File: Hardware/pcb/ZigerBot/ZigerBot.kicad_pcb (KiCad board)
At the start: 2 copper layers, 34 parts, among them J1 Screw_Terminal_01x03, J2 Screw_Terminal_01x02, J3 Screw_Terminal_01x02, U1 L7805, U2 NXP 74HC04, U3 L298P

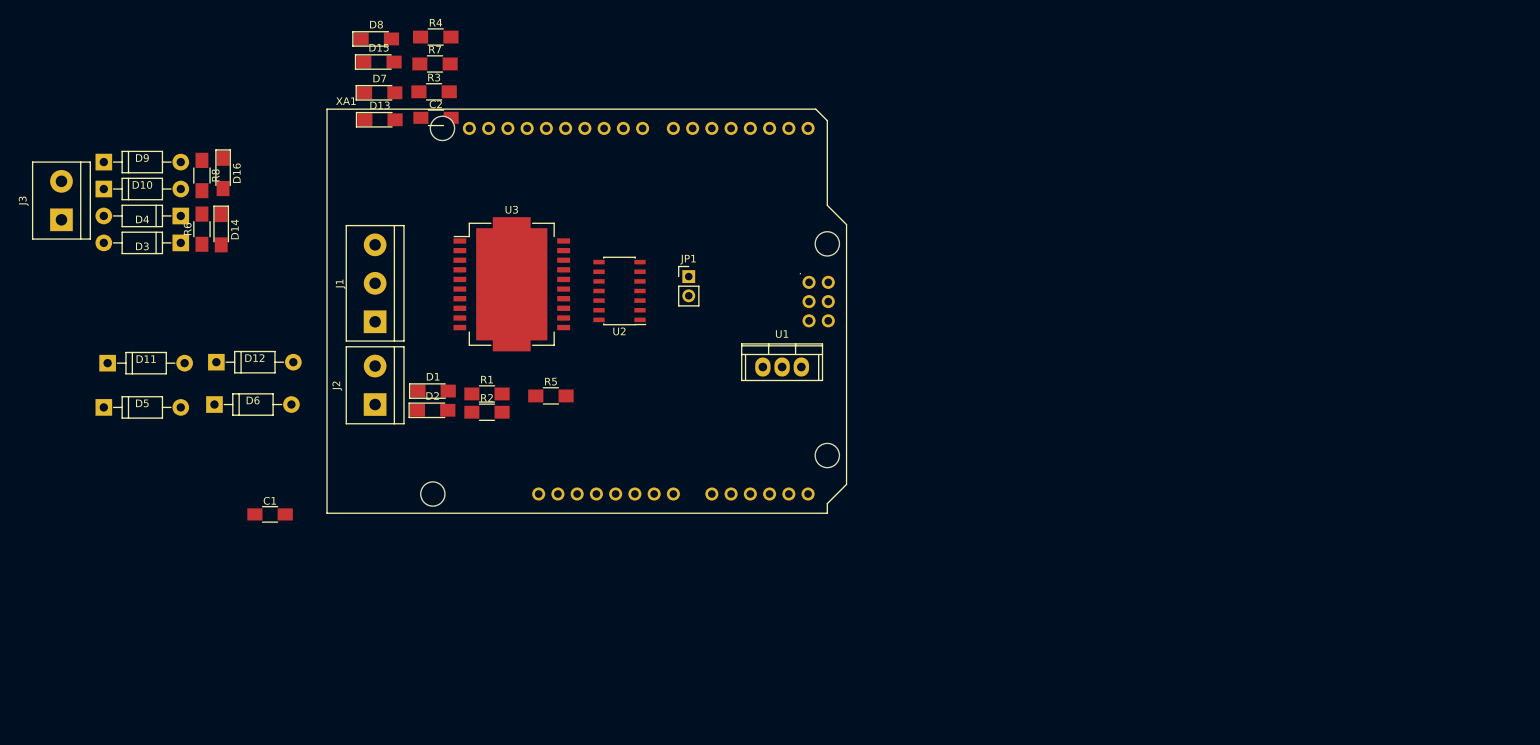
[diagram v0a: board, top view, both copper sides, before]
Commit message: PCB erweitert
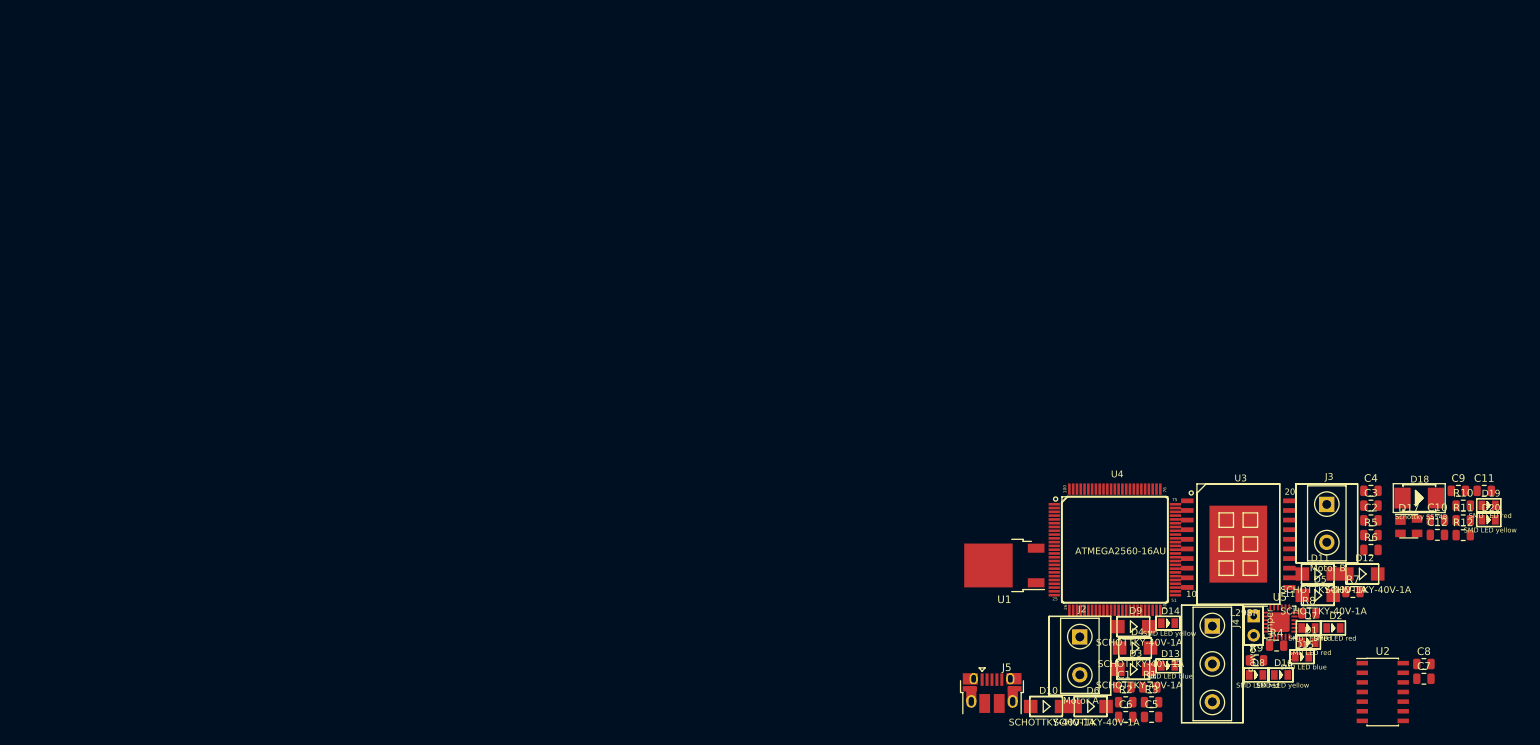
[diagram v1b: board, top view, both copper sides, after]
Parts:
- removed JP1: Jumper, Pin_Headers:Pin_Header_Straight_1x02_Pitch2.54mm
- removed XA1: Arduino_Uno_Shield, Arduino:Arduino_Uno_Shield
- added C10: 0.1uF, Capacitor_SMD:C_0805_2012Metric, F.Cu at (188.7, 87.4)
- added C11: 0.1uF, Capacitor_SMD:C_0805_2012Metric, F.Cu at (194.9, 83.5)
- added C12: 0.1uF, Capacitor_SMD:C_0805_2012Metric, F.Cu at (188.7, 89.3)
- added C3: 4.7uF, Capacitor_SMD:C_0805_2012Metric, F.Cu at (180.0, 85.5)
- added C4: 0.1uF, Capacitor_SMD:C_0805_2012Metric, F.Cu at (180.0, 83.5)
- added C5: 0.1uF, Capacitor_SMD:C_0805_2012Metric, F.Cu at (151.0, 113.4)
- added C6: 4.7uF, Capacitor_SMD:C_0805_2012Metric, F.Cu at (147.6, 113.4)
- added C7: 0.33uF, Capacitor_SMD:C_0805_2012Metric, F.Cu at (187.0, 108.3)
- added C8: 0.1uF, Capacitor_SMD:C_0805_2012Metric, F.Cu at (187.0, 106.4)
- added C9: 0.1uF, Capacitor_SMD:C_0805_2012Metric, F.Cu at (191.5, 83.5)
- added D17: SP0503BAHT, Package_TO_SOT_SMD:SOT-143, F.Cu at (185.0, 88.2)
- added D18: Schottky SS54B, SeeedOPL-Diode:DO-214AA, F.Cu at (186.3, 84.5)
- added D19: SMD LED red, SeeedOPL-LED:LED-0805, F.Cu at (195.5, 85.5)
- added D20: SMD LED yellow, SeeedOPL-LED:LED-0805, F.Cu at (195.5, 87.4)
- added J4: Jumper, SeeedOPL-Connector:H2-2.54, F.Cu at (164.5, 101.3)
- added J5: USB_B_Micro, Connector_USB:USB_Micro-B_Amphenol_10103594-0001LF_Horizontal, F.Cu at (130.0, 110.2)
- added R10: 10k, Resistor_SMD:R_0805_2012Metric, F.Cu at (192.1, 85.5)
- added R11: 10k, Resistor_SMD:R_0805_2012Metric, F.Cu at (192.1, 87.4)
- added R12: 10k, Resistor_SMD:R_0805_2012Metric, F.Cu at (192.1, 89.4)
- added R9: 1k, Resistor_SMD:R_0805_2012Metric, F.Cu at (164.9, 105.9)
- added U4: ATMEGA2560-16AU, SeeedOPL-IC:TQFP100-0.5-14X14MM, F.Cu at (146.2, 91.3)
- added U5: CP2102N-A01-GQFN24, Package_DFN_QFN:QFN-24-1EP_4x4mm_P0.5mm_EP2.6x2.6mm, F.Cu at (167.9, 100.9)
- C1, C2: value 0.1uF C1206S104M5RACTU -> 0.1uF; footprint Capacitors_SMD:C_1206_HandSoldering -> Capacitor_SMD:C_0805_2012Metric
- D1: value LED Blue -> SMD LED red; footprint LEDs:LED_1206_HandSoldering -> SeeedOPL-LED:LED-0805
- D10, D11, D12, D3, D4, D5, D6, D9: value SR140 -> SCHOTTKY-40V-1A; footprint ZigerBot:D_DO-41_SOD81_P10.16mm_Horizontal -> SeeedOPL-Diode:DO-214AC
- D13, D15: value LED Red -> SMD LED blue; footprint LEDs:LED_1206_HandSoldering -> SeeedOPL-LED:LED-0805
- D14: value LED BLUE -> SMD LED yellow; footprint LEDs:LED_1206_HandSoldering -> SeeedOPL-LED:LED-0805
- D16: value LED Yellow -> SMD LED yellow; footprint LEDs:LED_1206_HandSoldering -> SeeedOPL-LED:LED-0805
- D2: value LED Yellow -> SMD LED red; footprint LEDs:LED_1206_HandSoldering -> SeeedOPL-LED:LED-0805
- D7, D8: value LED Red -> SMD LED red; footprint LEDs:LED_1206_HandSoldering -> SeeedOPL-LED:LED-0805
- J1: value Screw_Terminal_01x03 -> Power; footprint Connectors_Terminal_Blocks:TerminalBlock_bornier-3_P5.08mm -> SeeedOPL-Connector:H3-5.0-15.5X8.0MM
- J2: value Screw_Terminal_01x02 -> Motor A; footprint Connectors_Terminal_Blocks:TerminalBlock_bornier-2_P5.08mm -> SeeedOPL-Connector:H2-5.0-10.5X8.0MM
- J3: value Screw_Terminal_01x02 -> Motor B; footprint Connectors_Terminal_Blocks:TerminalBlock_bornier-2_P5.08mm -> SeeedOPL-Connector:H2-5.0-10.5X8.0MM
- R1, R2, R3, R4, R5, R6, R7, R8: footprint Resistors_SMD:R_1206_HandSoldering -> Resistor_SMD:R_0805_2012Metric
- U1: value L7805 -> L7805CV; footprint Power_Integrations:TO-220 -> Package_TO_SOT_SMD:TO-252-2
- U2: footprint Housings_SOIC:SOIC-14_3.9x8.7mm_Pitch1.27mm -> Package_SO:SOIC-14_3.9x8.7mm_P1.27mm
- U3: footprint Housings_SOIC:HSOP-20-1EP_11.0x15.9mm_Pitch1.27mm_SlugDown -> SeeedOPL-IC:SOIC20G-1.27-16X11MM
- moved J3 171.8 mm to (174.1, 87.8), turned to 0 degrees
- moved D5 162.2 mm to (172.9, 97.3)
- moved D11 162.1 mm to (172.9, 94.5)
- moved R6 160.0 mm to (180.0, 91.3), turned to 0 degrees
- moved R8 157.1 mm to (171.8, 99.7), turned to 0 degrees
- moved D16 154.6 mm to (168.1, 107.8), turned to 0 degrees
- moved D12 153.8 mm to (178.8, 94.5)
- moved D9 149.1 mm to (148.6, 101.5)
- moved D15 145.0 mm to (170.9, 105.4)
- moved D8 143.3 mm to (164.8, 107.8)
- moved D10 141.9 mm to (137.1, 112.0)
- moved D7 141.5 mm to (171.7, 101.6)
- moved R7 139.8 mm to (177.6, 96.9)
- moved D4 138.3 mm to (148.8, 104.3), turned to 0 degrees
- moved D3 137.8 mm to (148.6, 107.1), turned to 0 degrees
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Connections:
- C1 pad 1: VSS -> GND
- C1 pad 2: GND -> /VSS
- C2 pad 1: /VS -> Net-(C2-Pad1)
- C2 pad 2: GND -> /VSS
- D10 pad 2: GND -> Net-(D10-Pad2)
- D11 pad 1: Net-(D1-Pad1) -> GND
- D11 pad 2: GND -> Net-(D11-Pad2)
- D12 pad 1: Net-(D12-Pad1) -> Net-(D11-Pad2)
- D12 pad 2: GND -> /VSS
- D3 pad 1: VSS -> GND
- D3 pad 2: Net-(D14-Pad1) -> Net-(D15-Pad-)
- D4 pad 1: VSS -> Net-(D15-Pad-)
- D4 pad 2: Net-(D10-Pad1) -> /VSS
- D5 pad 1: VSS -> GND
- D5 pad 2: Net-(D1-Pad1) -> Net-(D5-Pad2)
- D6 pad 1: VSS -> Net-(D5-Pad2)
- D6 pad 2: Net-(D12-Pad1) -> Net-(D6-Pad2)
- D9 pad 1: Net-(D14-Pad1) -> GND
- D9 pad 2: GND -> Net-(D10-Pad1)
- J1 pad 2: VSS -> /VSS
- J2 pad 1: Net-(D12-Pad1) -> Net-(D11-Pad2)
- J2 pad 2: Net-(D1-Pad1) -> Net-(D10-Pad1)
- J3 pad 1: Net-(D10-Pad1) -> Net-(D5-Pad2)
- J3 pad 2: Net-(D14-Pad1) -> Net-(D15-Pad-)
- R1 pad 1: Net-(D1-Pad2) -> /DirMotA
- R1 pad 2: Net-(D12-Pad1) -> Net-(D1-Pad+)
- R2 pad 1: Net-(D12-Pad1) -> /EnaMotA
- R2 pad 2: Net-(D2-Pad1) -> Net-(D2-Pad+)
- R3 pad 1: Net-(D7-Pad2) -> /DirMotB
- R3 pad 2: /D2 -> Net-(D7-Pad+)
- R4 pad 1: Net-(D8-Pad2) -> /EnaMotB
- R4 pad 2: /D3 -> Net-(D8-Pad+)
- R5 pad 1: Net-(D13-Pad2) -> Net-(D11-Pad2)
- R5 pad 2: /D4 -> Net-(D13-Pad+)
- R6 pad 1: Net-(D14-Pad2) -> Net-(D11-Pad2)
- R6 pad 2: Net-(D10-Pad1) -> Net-(D14-Pad-)
- R7 pad 1: Net-(D15-Pad2) -> Net-(D5-Pad2)
- R7 pad 2: /D11 -> Net-(D15-Pad+)
- R8 pad 1: Net-(D16-Pad1) -> Net-(D5-Pad2)
- R8 pad 2: Net-(D10-Pad1) -> Net-(D16-Pad-)
- U1 pad 3: VSS -> /VSS
- U2 pad 1: /D2 -> /DirMotA
- U2 pad 14: VSS -> /VSS
- U2 pad 3: /D4 -> /DirMotB
- U3 pad 12: VSS -> /VSS
- U3 pad 13: /D4 -> /DirMotB
- U3 pad 14: /D11 -> /EnaMotB
- U3 pad 16: Net-(D10-Pad1) -> Net-(D5-Pad2)
- U3 pad 17: Net-(D14-Pad1) -> Net-(D15-Pad-)
- U3 pad 4: Net-(D12-Pad1) -> Net-(D11-Pad2)
- U3 pad 5: Net-(D1-Pad1) -> Net-(D10-Pad1)
- U3 pad 6: /VS -> Net-(C4-Pad2)
- U3 pad 7: /D2 -> /DirMotA
- U3 pad 8: /D3 -> /EnaMotA
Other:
- rule pad_to_mask_clearance: 0.2 -> 0

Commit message: PCB changed
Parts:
- removed J5: USB_B_Micro, Connector_USB:USB_Micro-B_Amphenol_10103594-0001LF_Horizontal
- removed U1: L7805CV, Package_TO_SOT_SMD:TO-252-2
- removed U2: NXP 74HC04, Package_SO:SOIC-14_3.9x8.7mm_P1.27mm
- removed U5: CP2102N-A01-GQFN24, Package_DFN_QFN:QFN-24-1EP_4x4mm_P0.5mm_EP2.6x2.6mm
- added BZ1: Buzzer CEM-1203(42), ZigerBot:BUZZER_CEM-1203(24)_12mm_6.5mm_0.6mm, F.Cu at (43.7, 126.0)
- added C13: 100nF, Capacitors_SMD:C_0402, F.Cu at (146.5, 79.7)
- added C14: 100nF, Capacitors_SMD:C_0402, F.Cu at (149.5, 79.7)
- added C15: 100nF, Capacitors_SMD:C_0402, F.Cu at (160.1, 69.2)
- added C16: 100nF, Capacitors_SMD:C_0402, F.Cu at (152.4, 80.7)
- added C17: 100nF, Capacitors_SMD:C_0402, F.Cu at (163.1, 69.2)
- added C18: 100nF, Capacitors_SMD:C_0402, F.Cu at (160.1, 72.7)
- added C19: 100nF, Capacitors_SMD:C_0402, F.Cu at (148.4, 83.1)
- added C20: 100nF, Capacitors_SMD:C_0402, F.Cu at (140.7, 88.8)
- added C21: 0.1uF, Capacitors_SMD:C_0402, F.Cu at (143.7, 86.5)
- added C22: 4.7uF, Capacitors_SMD:C_0402, F.Cu at (137.8, 92.2)
- added C23: 100nF, Capacitors_SMD:C_0402, F.Cu at (156.3, 68.2)
- added C24: 100nF, Capacitors_SMD:C_0402, F.Cu at (134.8, 91.2)
- added C25: 100nF, Capacitors_SMD:C_0402, F.Cu at (149.6, 76.2)
- added C26: 100nF, Capacitors_SMD:C_0402, F.Cu at (145.4, 83.1)
- added C27: 100nF, Capacitors_SMD:C_0402, F.Cu at (140.5, 78.6)
- added C28: 100nF, Capacitors_SMD:C_0402, F.Cu at (131.8, 91.2)
- added C29: 100nF, Capacitors_SMD:C_0402, F.Cu at (149.6, 72.8)
- added C30: 100nF, Capacitors_SMD:C_0402, F.Cu at (143.5, 79.7)
- added C31: 100nF, Capacitors_SMD:C_0402, F.Cu at (146.6, 76.2)
- added C32: 100nF, Capacitors_SMD:C_0402, F.Cu at (161.0, 62.4)
- added C33: 0.1uF, Capacitors_SMD:C_0402, F.Cu at (164.1, 59.0)
- added C34: 4.7uF, Capacitors_SMD:C_0402, F.Cu at (140.5, 82.0)
- added C35: 100nF, Capacitors_SMD:C_0402, F.Cu at (158.0, 64.7)
- added C36: 100nF, Capacitors_SMD:C_0402, F.Cu at (135.8, 87.7)
- added C37: 100nF, Capacitors_SMD:C_0402, F.Cu at (153.3, 70.5)
- added C38: 100nF, Capacitors_SMD:C_0402, F.Cu at (125.9, 90.7)
- added C39: 100nF, Capacitors_SMD:C_0402, F.Cu at (158.0, 61.3)
- added D21: WS2812B, ZigerBot:LED_WS2812B-PLCC4, F.Cu at (200.2, 81.5)
- added D22: WS2812B, ZigerBot:LED_WS2812B-PLCC4, F.Cu at (208.0, 81.5)
- added D24: WS2812B, ZigerBot:LED_WS2812B-PLCC4, F.Cu at (176.5, 89.2)
- added D25: WS2812B, ZigerBot:LED_WS2812B-PLCC4, F.Cu at (184.4, 89.2)
- added D26: WS2812B, ZigerBot:LED_WS2812B-PLCC4, F.Cu at (192.3, 89.2)
- added D27: WS2812B, ZigerBot:LED_WS2812B-PLCC4, F.Cu at (200.2, 89.2)
- added D28: WS2812B, ZigerBot:LED_WS2812B-PLCC4, F.Cu at (208.0, 89.2)
- added D29: WS2812B, ZigerBot:LED_WS2812B-PLCC4, F.Cu at (176.5, 96.8)
- added D30: WS2812B, ZigerBot:LED_WS2812B-PLCC4, F.Cu at (184.4, 96.8)
- added D31: WS2812B, ZigerBot:LED_WS2812B-PLCC4, F.Cu at (192.3, 96.8)
- added D32: WS2812B, ZigerBot:LED_WS2812B-PLCC4, F.Cu at (200.2, 96.8)
- added D33: WS2812B, ZigerBot:LED_WS2812B-PLCC4, F.Cu at (208.0, 96.8)
- added J6: 3 Pin Male Servo Header, Pin_Headers:Pin_Header_Straight_1x03_Pitch2.54mm, F.Cu at (177.3, 112.3)
- added J7: 3 Pin Male Servo Header, Pin_Headers:Pin_Header_Straight_1x03_Pitch2.54mm, F.Cu at (189.0, 112.3)
- added J8: 3 Pin Male Servo Header, Pin_Headers:Pin_Header_Straight_1x03_Pitch2.54mm, F.Cu at (199.9, 112.3)
- added J9: 3 Pin Male Servo Header, Pin_Headers:Pin_Header_Straight_1x03_Pitch2.54mm, F.Cu at (209.6, 112.3)
- added JP1: Jumper, Pin_Headers:Pin_Header_Straight_1x03_Pitch2.54mm, F.Cu at (112.3, 68.3)
- added Q1: SMD-MOSFET-P-CH-20V-2A-FDN340P_SOT-23_, TO_SOT_Packages_SMD:SOT-23, F.Cu at (82.4, 87.0)
- added RV1: Potentiometer, Potentiometers:Potentiometer_Trimmer-EVM3E, F.Cu at (136.8, 79.5)
- added RV2: Potentiometer, Potentiometers:Potentiometer_Trimmer-EVM3E, F.Cu at (154.3, 62.2)
- added SW1: SMD Button, Buttons_Switches_SMD:SW_SPST_SKQG, F.Cu at (113.8, 106.7)
- added SW2: SMD Button, Buttons_Switches_SMD:SW_SPST_SKQG, F.Cu at (104.9, 106.7)
- added SW3: SMD Button, Buttons_Switches_SMD:SW_SPST_SKQG, F.Cu at (122.7, 106.7)
- added SW4: SMD Button, Buttons_Switches_SMD:SW_SPST_SKQG, F.Cu at (131.3, 106.7)
- added Y1: 16MHz Resonator, ZigerBot:Resonator_SMD_muRata_CSTNE16M0V530000_3pin_3.2x1.3x0.9mm, F.Cu at (82.5, 84.1)
- C1, C10, C8, C9: footprint Capacitor_SMD:C_0805_2012Metric -> Capacitors_SMD:C_0402
- C11, C12: value 0.1uF -> 100nF; footprint Capacitor_SMD:C_0805_2012Metric -> Capacitors_SMD:C_0402
- C2: value 0.1uF -> 0.33uF; footprint Capacitor_SMD:C_0805_2012Metric -> Capacitors_SMD:C_0402
- C3: value 4.7uF -> 0.1uF; footprint Capacitor_SMD:C_0805_2012Metric -> Capacitors_SMD:C_0402
- C4: value 0.1uF -> 0.1 uF; footprint Capacitor_SMD:C_0805_2012Metric -> Capacitors_SMD:C_0402
- C5: value 0.1uF -> 10uF 16V; footprint Capacitor_SMD:C_0805_2012Metric -> Capacitors_SMD:C_0402
- C6: value 4.7uF -> 10uF 16V; footprint Capacitor_SMD:C_0805_2012Metric -> Capacitors_SMD:C_0402
- C7: value 0.33uF -> 10uF 16V; footprint Capacitor_SMD:C_0805_2012Metric -> Capacitors_SMD:C_0402
- D1: footprint SeeedOPL-LED:LED-0805 -> ZigerBot:LED_0603
- D10, D11, D12, D9: value SCHOTTKY-40V-1A -> WS2812B; footprint SeeedOPL-Diode:DO-214AC -> ZigerBot:LED_WS2812B-PLCC4
- D13, D15: value SMD LED blue -> WS2812B; footprint SeeedOPL-LED:LED-0805 -> ZigerBot:LED_WS2812B-PLCC4
- D14, D16, D20: value SMD LED yellow -> WS2812B; footprint SeeedOPL-LED:LED-0805 -> ZigerBot:LED_WS2812B-PLCC4
- D17: value SP0503BAHT -> WS2812B; footprint Package_TO_SOT_SMD:SOT-143 -> ZigerBot:LED_WS2812B-PLCC4
- D18: value Schottky SS54B -> WS2812B; footprint SeeedOPL-Diode:DO-214AA -> ZigerBot:LED_WS2812B-PLCC4
- D19, D8: value SMD LED red -> WS2812B; footprint SeeedOPL-LED:LED-0805 -> ZigerBot:LED_WS2812B-PLCC4
- D2: value SMD LED red -> SMD LED blue; footprint SeeedOPL-LED:LED-0805 -> ZigerBot:LED_0603
- D3, D4: value SCHOTTKY-40V-1A -> SMD LED yellow; footprint SeeedOPL-Diode:DO-214AC -> ZigerBot:LED_0603
- D5: value SCHOTTKY-40V-1A -> SMD LED green FAULT; footprint SeeedOPL-Diode:DO-214AC -> ZigerBot:LED_0603
- D6: value SCHOTTKY-40V-1A -> SMD LED blue; footprint SeeedOPL-Diode:DO-214AC -> ZigerBot:LED_0603
- D7: value SMD LED red -> SMD LED yellow; footprint SeeedOPL-LED:LED-0805 -> ZigerBot:LED_0603
- J1: value Power -> Motor A; footprint SeeedOPL-Connector:H3-5.0-15.5X8.0MM -> SeeedOPL-Connector:H2-5.0-10.5X8.0MM
- J2: value Motor A -> M Power
- J4: value Jumper -> 4 Pin Male SR-04 Header; footprint SeeedOPL-Connector:H2-2.54 -> SeeedOPL-Connector:H4-2.54
- R1: value 1k -> 100 Ohm; footprint Resistor_SMD:R_0805_2012Metric -> Resistors_SMD:R_0402
- R10, R11, R12: value 10k -> 1k; footprint Resistor_SMD:R_0805_2012Metric -> Resistors_SMD:R_0402
- R2, R3, R6, R9: value 1k -> 10k; footprint Resistor_SMD:R_0805_2012Metric -> Resistors_SMD:R_0402
- R4, R5: footprint Resistor_SMD:R_0805_2012Metric -> Resistors_SMD:R_0402
- R7, R8: value 1k -> 0.2 Ohm; footprint Resistor_SMD:R_0805_2012Metric -> Resistors_SMD:R_0402
- U3: value L298P -> ATmega2560-16AU; footprint SeeedOPL-IC:SOIC20G-1.27-16X11MM -> SeeedOPL-IC:TQFP100-0.5-14X14MM
- U4: value ATMEGA2560-16AU -> CP2102N-A01-GQFN24; footprint SeeedOPL-IC:TQFP100-0.5-14X14MM -> Housings_DFN_QFN:QFN-24-1EP_4x4mm_Pitch0.5mm
- moved R5 77.8 mm to (102.7, 80.8)
- moved D1 77.3 mm to (95.1, 93.4)
- moved D7 73.8 mm to (98.4, 93.4)
- moved D10 71.7 mm to (192.3, 66.3)
- moved J3 70.3 mm to (231.6, 47.5)
- moved J1 61.0 mm to (150.6, 45.9)
- moved J4 61.0 mm to (120.5, 59.0)
- moved C8 60.2 mm to (128.8, 90.7)
- moved C7 53.9 mm to (143.6, 76.2)
- moved R2 51.5 mm to (163.4, 62.4)
- moved U3 50.4 mm to (191.0, 49.0)
- moved D9 50.2 mm to (184.4, 66.3)
- moved J2 47.5 mm to (97.6, 87.1)
- moved C3 47.1 mm to (132.9, 84.3)
- moved D16 46.7 mm to (200.2, 73.9)
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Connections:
- C1 pad 1: GND -> Net-(C1-Pad1)
- C1 pad 2: /VSS -> /DTRmega
- C10 pad 2: Net-(C10-Pad2) -> 5V
- C11 pad 1: Net-(C11-Pad1) -> GND
- C11 pad 2: Net-(C10-Pad2) -> 5V
- C12 pad 2: Net-(C10-Pad2) -> 5V
- C2 pad 2: /VSS -> Net-(C2-Pad2)
- C3 pad 1: Net-(C2-Pad1) -> 5V
- C3 pad 2: /VSS -> Net-(C2-Pad1)
- C4 pad 1: GND -> /VCP
- C5 pad 1: Net-(C2-Pad1) -> Net-(C4-Pad2)
- C5 pad 2: Net-(C5-Pad2) -> Net-(C2-Pad1)
- C6 pad 1: Net-(C2-Pad1) -> Net-(C4-Pad2)
- C6 pad 2: Net-(C5-Pad2) -> Net-(C2-Pad1)
- C8 pad 1: /VSS -> 5V
- C9 pad 1: Net-(C9-Pad1) -> GND
- C9 pad 2: /DTRmega -> 5V
- D10 pad 1: Net-(D10-Pad1) -> 5V
- D11 pad 1: GND -> 5V
- D12 pad 1: Net-(D11-Pad2) -> 5V
- D12 pad 2: /VSS -> Net-(D12-Pad2)
- D17 pad 1: GND -> 5V
- D17 pad 3: Net-(D17-Pad3) -> GND
- D17 pad 4: /VSS -> Net-(D16-Pad2)
- D3 pad 1: GND -> Net-(D3-Pad1)
- D3 pad 2: Net-(D15-Pad-) -> Net-(D2-Pad1)
- D4 pad 1: Net-(D15-Pad-) -> (no net)
- D4 pad 2: /VSS -> (no net)
- D5 pad 1: GND -> (no net)
- D5 pad 2: Net-(D5-Pad2) -> (no net)
- D6 pad 1: Net-(D5-Pad2) -> Net-(D6-Pad1)
- D9 pad 1: GND -> 5V
- D9 pad 2: Net-(D10-Pad1) -> Net-(D10-Pad4)
- J1 pad 1: GND -> Net-(D2-Pad1)
- J1 pad 2: /VSS -> Net-(D2-Pad1)
- J2 pad 1: Net-(D11-Pad2) -> GND
- J2 pad 2: Net-(D10-Pad1) -> Net-(C2-Pad2)
- J3 pad 1: Net-(D5-Pad2) -> Net-(J3-Pad1)
- J3 pad 2: Net-(D15-Pad-) -> Net-(D6-Pad1)
- J4 pad 1: Net-(C4-Pad2) -> 5V
- J4 pad 2: Net-(C7-Pad2) -> /Trig
- R1 pad 1: /DirMotA -> /Buzz
- R1 pad 2: Net-(D1-Pad+) -> Net-(BZ1-Pad1)
- R10 pad 1: /VSS -> Net-(J3-Pad1)
- R10 pad 2: Net-(D19-Pad+) -> Net-(D6-Pad2)
- R11 pad 1: Net-(C10-Pad2) -> Net-(J3-Pad1)
- R11 pad 2: Net-(C9-Pad1) -> Net-(D7-Pad1)
- R12 pad 1: /D13 -> Net-(R12-Pad1)
- R12 pad 2: Net-(D20-Pad+) -> Net-(R12-Pad2)
- R2 pad 1: /EnaMotA -> 5V
- R2 pad 2: Net-(D2-Pad+) -> Net-(D1-Pad+)
- R3 pad 1: /DirMotB -> 5V
- R3 pad 2: Net-(D7-Pad+) -> Net-(C1-Pad1)
- R4 pad 1: /EnaMotB -> Net-(R4-Pad1)
- R4 pad 2: Net-(D8-Pad+) -> Net-(D2-Pad2)
- R5 pad 1: Net-(D11-Pad2) -> Net-(R4-Pad1)
- R5 pad 2: Net-(D13-Pad+) -> Net-(D3-Pad1)
- R6 pad 1: Net-(D11-Pad2) -> /D13
- R6 pad 2: Net-(D14-Pad-) -> Net-(D4-Pad+)
- R7 pad 1: Net-(D5-Pad2) -> Net-(R7-Pad1)
- R7 pad 2: Net-(D15-Pad+) -> Net-(C2-Pad1)
- R8 pad 1: Net-(D5-Pad2) -> Net-(R8-Pad1)
- R8 pad 2: Net-(D16-Pad-) -> Net-(C2-Pad1)
- U3 pad 1: GND -> Net-(U3-Pad1)
- U3 pad 10: GND -> 5V
- U3 pad 12: /VSS -> Net-(U3-Pad12)
- U3 pad 13: /DirMotB -> Net-(U3-Pad13)
- U3 pad 14: /EnaMotB -> Net-(U3-Pad14)
- U3 pad 16: Net-(D5-Pad2) -> Net-(U3-Pad16)
- U3 pad 17: Net-(D15-Pad-) -> Net-(U3-Pad17)
- U3 pad 2: Net-(U3-Pad2) -> /RXmega
- U3 pad 20: GND -> Net-(U3-Pad20)
- U3 pad 3: Net-(U3-Pad3) -> /TXmega
- U3 pad 4: Net-(D11-Pad2) -> Net-(U3-Pad4)
- U3 pad 5: Net-(D10-Pad1) -> Net-(U3-Pad5)
- U3 pad 6: Net-(C4-Pad2) -> Net-(U3-Pad6)
- U3 pad 7: /DirMotA -> Net-(U3-Pad7)
- U3 pad 8: /EnaMotA -> Net-(U3-Pad8)
- U4 pad 10: Net-(C10-Pad2) -> Net-(C21-Pad1)
- U4 pad 11: GND -> Net-(U4-Pad11)
- U4 pad 16: Net-(U4-Pad16) -> Net-(C21-Pad1)
- U4 pad 2: /RXmega -> Net-(C21-Pad1)
- U4 pad 20: Net-(U4-Pad20) -> /TXmega
- U4 pad 21: Net-(U4-Pad21) -> /RXmega
- U4 pad 23: Net-(U4-Pad23) -> /DTRmega
- U4 pad 25: Net-(U4-Pad25) -> Net-(C21-Pad1)
- U4 pad 3: /TXmega -> Net-(D23-Pad3)
- U4 pad 5: Net-(U4-Pad5) -> Net-(R12-Pad1)
- U4 pad 7: Net-(U4-Pad7) -> 5V
- U4 pad 8: Net-(U4-Pad8) -> 5V
- U4 pad 9: Net-(U4-Pad9) -> Net-(R12-Pad2)

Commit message: Updated Package Info
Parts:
- added D23: SP0503BAHT, TO_SOT_Packages_SMD:SOT-143_Handsoldering, F.Cu at (158.9, 24.3)
- added J5: USB_B_Micro, Connectors_USB:USB_Micro-B_Molex-105017-0001, F.Cu at (171.0, 18.9)
- added U1: L7805CDT-TR, TO_SOT_Packages_SMD:TO-252-2, F.Cu at (161.0, 19.0)
- added U2: DRV8833PW, Housings_SSOP:TSSOP-16-1EP_4.4x5mm_Pitch0.65mm, F.Cu at (170.1, 24.6)
- U3: footprint SeeedOPL-IC:TQFP100-0.5-14X14MM -> Housings_QFP:TQFP-100_14x14mm_Pitch0.5mm
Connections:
- D1 pad 1: (no net) -> GND
- D1 pad 2: (no net) -> Net-(D1-Pad2)
- D4 pad 1: (no net) -> GND
- D4 pad 2: (no net) -> Net-(D4-Pad2)
- D5 pad 1: (no net) -> GND
- D5 pad 2: (no net) -> Net-(D5-Pad2)
- R2 pad 2: Net-(D1-Pad+) -> Net-(D1-Pad2)
- R6 pad 2: Net-(D4-Pad+) -> Net-(D4-Pad2)
- R9 pad 2: Net-(D5-Pad+) -> Net-(D5-Pad2)
